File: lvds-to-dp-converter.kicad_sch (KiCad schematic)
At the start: 37 parts, among them U23 SN65DSI86ZXHR, U24 TLV73312PDBVT, U25 TLV73318PDBVT, U26 TLV73312PDBVT, Y3 Oscillator_12MHz_ESC_2520MV

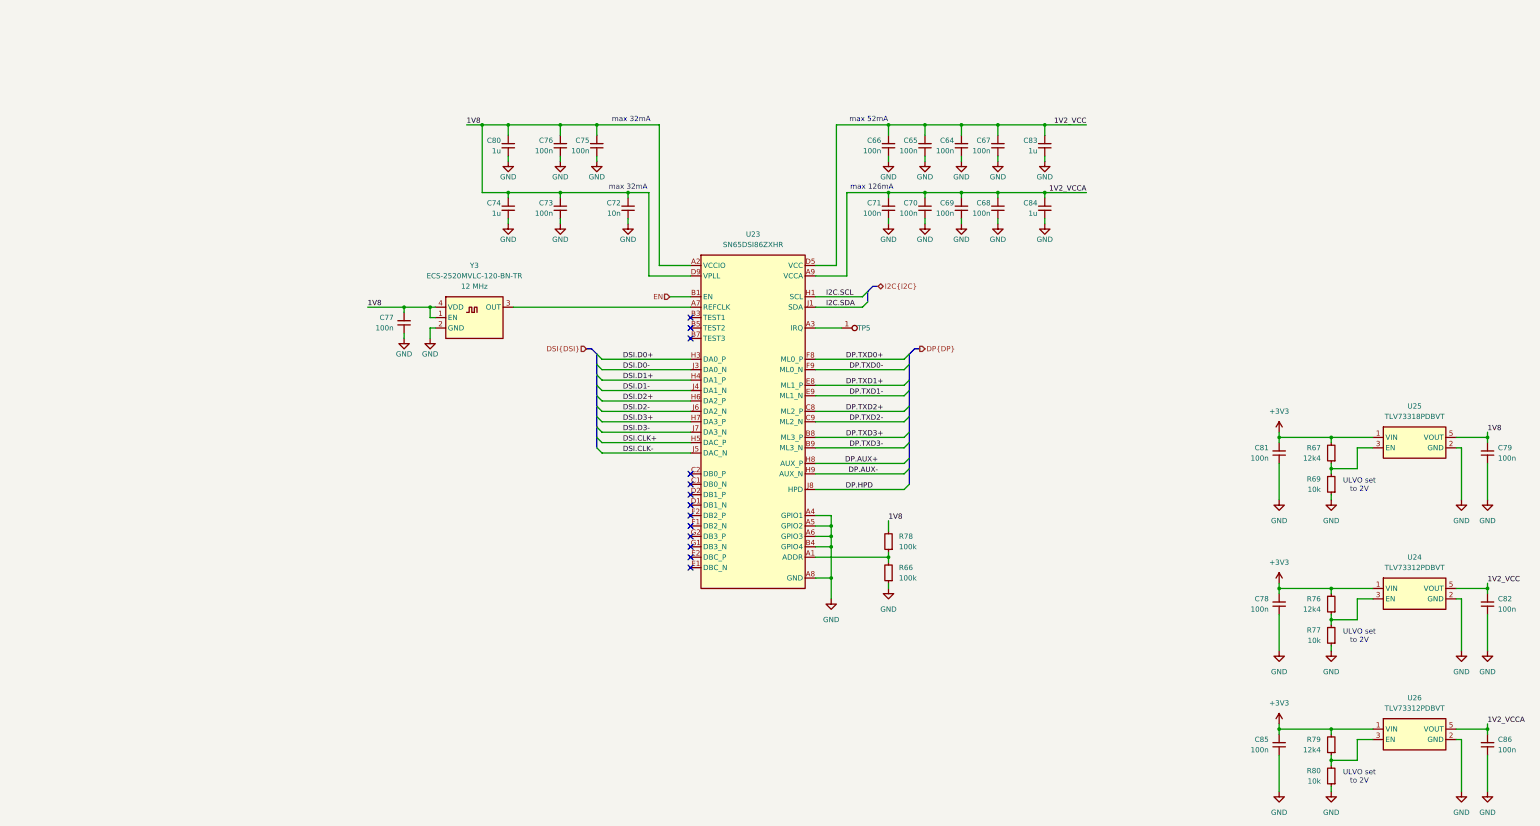
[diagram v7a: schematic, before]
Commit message: [#82687] Add IT6251 to schematic
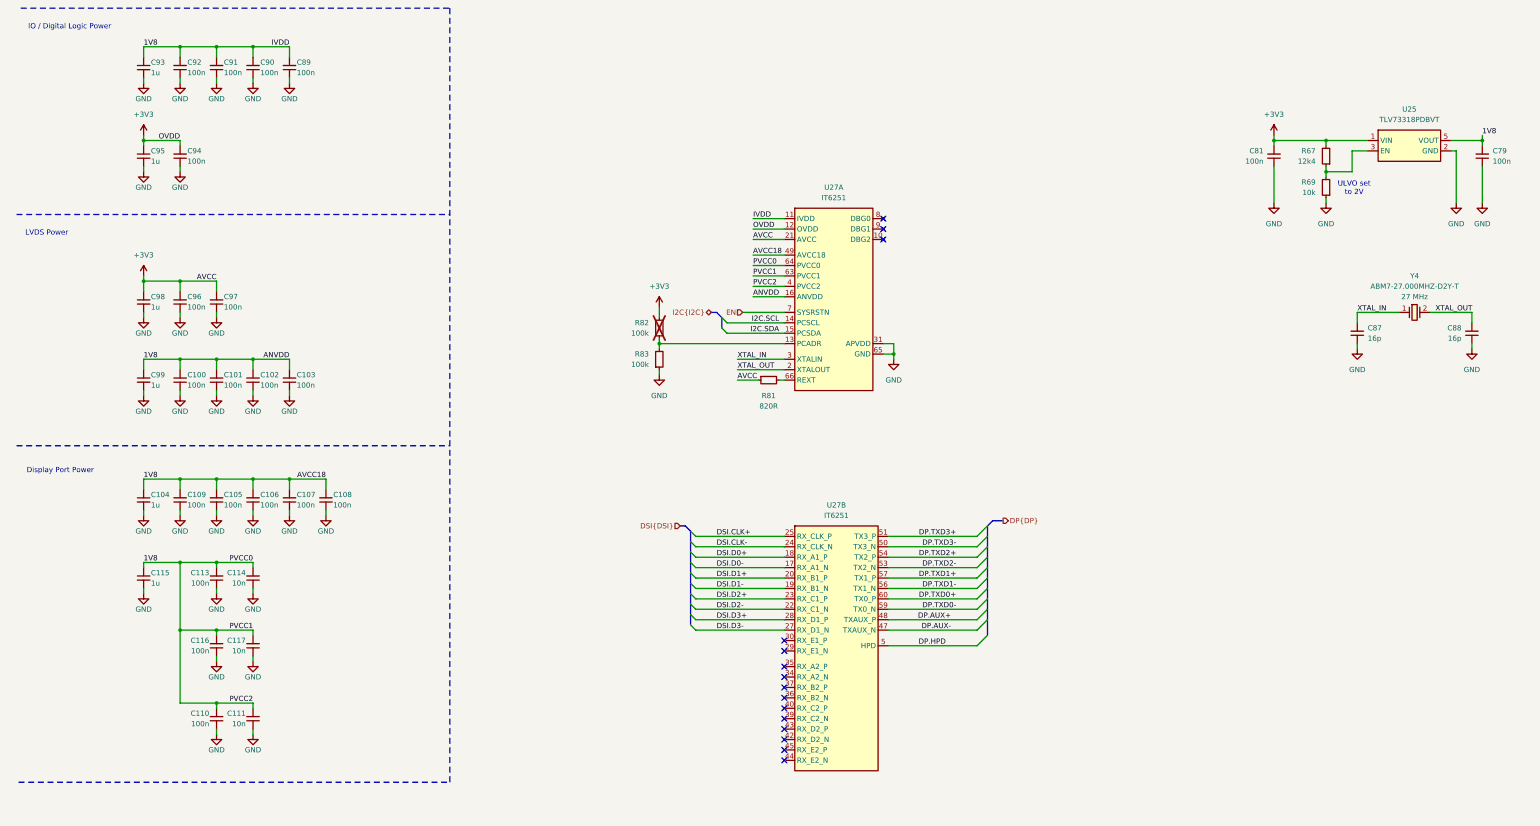
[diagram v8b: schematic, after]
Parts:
- removed C64, C65, C66, C67, C68, C69, C70, C71, C73, C75, C76, C78, C82, C85, C86: C_100n_0402, antmicro-footprints:C_0402_1005Metric, symbol antmicroCapacitors0402:C_100n_0402
- removed C72: C_10n_0402, antmicro-footprints:C_0402_1005Metric, symbol antmicroCapacitors0402:C_10n_0402
- removed C74, C80, C83, C84: C_1u_0402, antmicro-footprints:C_0402_1005Metric, symbol antmicroCapacitors0402:C_1u_0402
- removed C77: C_100n_0402, antmicro-footprints:C_0402_1005Metric, symbol Capacitors0402:C_100n_0402
- removed R66, R78: R_100k_0402, antmicro-footprints:R_0402_1005Metric, symbol antmicroResistors0402:R_100k_0402
- removed R76, R79: R_12k4_0402, antmicro-footprints:R_0402_1005Metric, symbol antmicroResistors0402:R_12k4_0402
- removed R77, R80: R_10k_0402, antmicro-footprints:R_0402_1005Metric, symbol antmicroResistors0402:R_10k_0402
- removed TP5: TP_0.75mm_SMD, antmicro-footprints:TP_SMD_0.75mm, symbol antmicroTestPoints:TP_0.75mm_SMD
- removed U23: SN65DSI86ZXHR, antmicro-footprints:NFBGA-64_5x5mm_Layout9X9_P0.5mm, symbol antmicroInterfaceControllers:SN65DSI86ZXHR
- removed U24, U26: TLV73312PDBVT, antmicro-footprints:SOT-23-5, symbol antmicroPMICVoltageRegulatorsLinear:TLV73312PDBVT
- removed Y3: Oscillator_12MHz_ESC_2520MV, antmicro-footprints:Oscillator_SMD_ECS_2520MV_2.5x2mm, symbol antmicroOscillators:Oscillator_12MHz_ESC_2520MV
- added C100, C101, C102, C103, C105, C106, C107, C108, C109, C110, C113, C116, C89, C90, C91, C92, C94, C96, C97: C_100n_0402, antmicro-footprints:C_0402_1005Metric, symbol antmicroCapacitors0402:C_100n_0402
- added C104, C115, C93, C95, C98, C99: C_1u_0402, antmicro-footprints:C_0402_1005Metric, symbol antmicroCapacitors0402:C_1u_0402
- added C111, C114, C117: C_10n_0402, antmicro-footprints:C_0402_1005Metric, symbol antmicroCapacitors0402:C_10n_0402
- added C87, C88: C_16p_0402, antmicro-footprints:C_0402_1005Metric, symbol antmicroCapacitors0402:C_16p_0402
- added R81: R_820R_0402, antmicro-footprints:R_0402_1005Metric, symbol antmicroResistors0402:R_820R_0402
- added R82, R83: R_100k_0402, antmicro-footprints:R_0402_1005Metric, symbol antmicroResistors0402:R_100k_0402
- added U27: IT6251, antmicro-footprints:QFN-64-1EP_9x9mm_P0.5mm, symbol antmicroInterfaceControllers:IT6251
- added Y4: Resonator_27MHz_ABM7, antmicro-footprints:Resonator_SMD_Abracon_ABM7_6x3.5x1.4mm, symbol antmicroResonators:Resonator_27MHz_ABM7
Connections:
- net +3V3: now also C94.2, C95.1, C96.2, C97.2, C98.1, R81.1, R82.2, U27.12 (OVDD), U27.21 (AVCC), U27.38 (AVCC)
- net DP.AUX+: now also U27.48 (TXAUX_P)
- net DP.AUX-: now also U27.47 (TXAUX_N)
- net DP.HPD: now also U27.5 (HPD)
- net DP.TXD0+: now also U27.60 (TX0_P)
- net DP.TXD0-: now also U27.59 (TX0_N)
- net DP.TXD1+: now also U27.57 (TX1_P)
- net DP.TXD1-: now also U27.56 (TX1_N)
- net DP.TXD2+: now also U27.54 (TX2_P)
- net DP.TXD2-: now also U27.53 (TX2_N)
- net DP.TXD3+: now also U27.51 (TX3_P)
- net DP.TXD3-: now also U27.50 (TX3_N)
- net DSI.CLK+: now also U27.25 (RX_CLK_P)
- net DSI.CLK-: now also U27.24 (RX_CLK_N)
- net DSI.D0+: now also U27.18 (RX_A1_P)
- net DSI.D0-: now also U27.17 (RX_A1_N)
- net DSI.D1+: now also U27.20 (RX_B1_P)
- net DSI.D1-: now also U27.19 (RX_B1_N)
- net DSI.D2+: now also U27.23 (RX_C1_P)
- net DSI.D2-: now also U27.22 (RX_C1_N)
- net DSI.D3+: now also U27.28 (RX_D1_P)
- net DSI.D3-: now also U27.27 (RX_D1_N)
- net EN: now also U27.7 (SYSRSTN)
- net GND: now also C100.1, C101.1, C102.1, C103.1, C104.2, C105.1, C106.1, C107.1, C108.1, C109.1, C110.1, C111.1, C113.1, C114.1, C115.2, C116.1, C117.1, C87.1, C88.1, C89.1, C90.1, C91.1, C92.1, C93.2, C94.1, C95.2, C96.1, C97.1, C98.2, C99.2, R83.1, U27.31 (APVDD), U27.65 (GND)
- net I2C.SCL: now also U27.14 (PCSCL)
- net I2C.SDA: now also U27.15 (PCSDA)
- net VCCIO renamed 1V8
- net 1V8: now also C100.2, C101.2, C102.2, C103.2, C104.1, C105.2, C106.2, C107.2, C108.2, C109.2, C110.2, C111.2, C113.2, C114.2, C115.1, C116.2, C117.2, C89.2, C90.2, C91.2, C92.2, C93.1, C99.1, U27.11 (IVDD), U27.16 (ANVDD), U27.26 (ANVDD), U27.32 (IVDD), U27.33 (ANVDD), U27.4 (PVCC2), U27.41 (ANVDD), U27.46 (IVDD), U27.49 (AVCC18), U27.52 (AVCC18), U27.55 (AVCC18), U27.58 (AVCC18), U27.6 (IVDD), U27.61 (AVCC18), U27.63 (PVCC1), U27.64 (PVCC0)
- new net: R82.1, R83.2, U27.13 (PCADR)
- new net: R81.2, U27.66 (REXT)
- new net XTAL_IN: C87.2, U27.3 (XTALIN), Y4.1
- new net XTAL_OUT: C88.2, U27.2 (XTALOUT), Y4.2
- no-connect marks 13 -> 15
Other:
- note added: "Display Port Power"
- note added: "IO / Digital Logic Power"
- note added: "LVDS Power"
- note removed: "max 126mA"
- note removed: "max 32mA"
- note removed: "max 52mA"
- moved on the sheet: C79, C81, R67, R69, U25
